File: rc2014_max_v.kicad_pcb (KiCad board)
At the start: 4 copper layers, 101.6 x 50.8 mm, 128 parts, among them J1 M3 Mounting Hole, J2 Conn_01x40, J3 Conn_01x24, J4 USB_B_Micro, J5 AVR-JTAG-10, J6 Pro Bus, J7 PMOD1, J8 PMOD2, J9 UPDI TTL, SW1 SW_Push, SW2 SW_Push, U1 TXB0108PWR, U10 ATtiny1614-SS, U11 5M1270ZT144C5N, U12 93LC46BT-I/OT, U13 IS61LV5128AL-10TLI, U14 Si5351A-B-GT, U15 TXB0108PWR, U16 TXB0108PWR, U18 MIC5356-SGYMME, U2 TXB0108PWR, U3 TXB0108PWR, U4 TXB0108PWR, U5 TXB0108PWR, U6 TXB0108PWR, U7 TXB0108PWR, U8 FT2232H, U9 TPD2EUSB30, X1 KC5032K12.0000C10E00, Y1 25MHZ 8PF

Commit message: formatting and layer stitching
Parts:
- moved U6 0.89 mm to (145.3, 117.3)
- moved U4 0.64 mm to (136.3, 117.3)
- moved R4 0.63 mm to (141.0, 115.1)
- moved C33 0.51 mm to (131.8, 117.3)
- moved U5 0.51 mm to (163.3, 117.3)
- moved U2 0.51 mm to (127.3, 117.3)
- moved J7 0.38 mm to (173.0, 102.9)
- moved R3 0.25 mm to (159.0, 115.1)
- moved J8 0.25 mm to (173.0, 86.1)
- moved R2 0.25 mm to (122.9, 115.1)
- moved RN1 0.25 mm to (122.2, 119.4)
- moved U7 0.13 mm to (154.3, 117.3)
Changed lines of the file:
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@@
   (page A4)
   (layers
-    (0 F.Cu signal)
-    (1 In1.Cu power hide)
+    (0 F.Cu signal hide)
+    (1 In1.Cu power)
     (2 In2.Cu power hide)
     (31 B.Cu signal)
@@
     (aux_axis_origin 0 0)
     (grid_origin 75.438 127.508)
-    (visible_elements FFFFFF7F)
+    (visible_elements FFFFF77F)
     (pcbplotparams
       (layerselection 0x010f0_ffffffff)
@@
     (add_net CLK)
     (add_net CLK2)
-    (add_net CLK2_F)
     (add_net CLK_100Mhz)
     (add_net CLK_1Mhz)
@@
     (add_net "Net-(D13-Pad4)")
     (add_net "Net-(D13-Pad5)")
-    (add_net "Net-(J2-Pad37)")
-    (add_net "Net-(J2-Pad38)")
-    (add_net "Net-(J2-Pad39)")
-    (add_net "Net-(J2-Pad40)")
-    (add_net "Net-(J3-Pad21)")
-    (add_net "Net-(J3-Pad22)")
-    (add_net "Net-(J3-Pad23)")
-    (add_net "Net-(J3-Pad24)")
     (add_net "Net-(J4-Pad2)")
     (add_net "Net-(J4-Pad3)")
-    (add_net "Net-(J5-Pad7)")
-    (add_net "Net-(J5-Pad8)")
     (add_net "Net-(LED1-Pad2)")
     (add_net "Net-(LED2-Pad2)")
@@
     (add_net "Net-(RN2-Pad3)")
     (add_net "Net-(RN2-Pad4)")
-    (add_net "Net-(RN3-Pad4)")
-    (add_net "Net-(RN3-Pad5)")
     (add_net "Net-(RN4-Pad1)")
     (add_net "Net-(RN4-Pad2)")
-    (add_net "Net-(RN4-Pad4)")
-    (add_net "Net-(RN5-Pad4)")
-    (add_net "Net-(U10-Pad11)")
-    (add_net "Net-(U10-Pad12)")
-    (add_net "Net-(U10-Pad13)")
-    (add_net "Net-(U10-Pad2)")
-    (add_net "Net-(U10-Pad3)")
-    (add_net "Net-(U10-Pad4)")
-    (add_net "Net-(U10-Pad5)")
-    (add_net "Net-(U10-Pad6)")
-    (add_net "Net-(U10-Pad7)")
-    (add_net "Net-(U11-Pad106)")
-    (add_net "Net-(U11-Pad119)")
-    (add_net "Net-(U11-Pad120)")
-    (add_net "Net-(U11-Pad121)")
-    (add_net "Net-(U11-Pad122)")
-    (add_net "Net-(U11-Pad129)")
-    (add_net "Net-(U11-Pad130)")
-    (add_net "Net-(U11-Pad131)")
-    (add_net "Net-(U11-Pad132)")
-    (add_net "Net-(U11-Pad133)")
-    (add_net "Net-(U11-Pad32)")
-    (add_net "Net-(U11-Pad72)")
-    (add_net "Net-(U13-Pad1)")
-    (add_net "Net-(U13-Pad2)")
-    (add_net "Net-(U13-Pad21)")
-    (add_net "Net-(U13-Pad22)")
-    (add_net "Net-(U13-Pad23)")
-    (add_net "Net-(U13-Pad24)")
-    (add_net "Net-(U13-Pad25)")
-    (add_net "Net-(U13-Pad39)")
-    (add_net "Net-(U13-Pad40)")
-    (add_net "Net-(U13-Pad41)")
-    (add_net "Net-(U13-Pad42)")
-    (add_net "Net-(U13-Pad43)")
-    (add_net "Net-(U13-Pad44)")
     (add_net "Net-(U14-Pad2)")
     (add_net "Net-(U14-Pad3)")
-    (add_net "Net-(U18-Pad3)")
-    (add_net "Net-(U18-Pad6)")
     (add_net "Net-(U8-Pad2)")
-    (add_net "Net-(U8-Pad21)")
-    (add_net "Net-(U8-Pad22)")
-    (add_net "Net-(U8-Pad23)")
-    (add_net "Net-(U8-Pad24)")
-    (add_net "Net-(U8-Pad26)")
-    (add_net "Net-(U8-Pad27)")
-    (add_net "Net-(U8-Pad28)")
-    (add_net "Net-(U8-Pad29)")
-    (add_net "Net-(U8-Pad3)")
-    (add_net "Net-(U8-Pad30)")
-    (add_net "Net-(U8-Pad32)")
-    (add_net "Net-(U8-Pad33)")
-    (add_net "Net-(U8-Pad34)")
-    (add_net "Net-(U8-Pad36)")
-    (add_net "Net-(U8-Pad38)")
-    (add_net "Net-(U8-Pad39)")
-    (add_net "Net-(U8-Pad40)")
-    (add_net "Net-(U8-Pad41)")
-    (add_net "Net-(U8-Pad43)")
-    (add_net "Net-(U8-Pad44)")
-    (add_net "Net-(U8-Pad45)")
-    (add_net "Net-(U8-Pad46)")
-    (add_net "Net-(U8-Pad48)")
-    (add_net "Net-(U8-Pad49)")
-    (add_net "Net-(U8-Pad50)")
-    (add_net "Net-(U8-Pad52)")
-    (add_net "Net-(U8-Pad53)")
-    (add_net "Net-(U8-Pad54)")
-    (add_net "Net-(U8-Pad55)")
-    (add_net "Net-(U8-Pad57)")
-    (add_net "Net-(U8-Pad58)")
-    (add_net "Net-(U8-Pad59)")
     (add_net OE_A)
     (add_net OE_C)
@@
   )
   (module Capacitor_SMD:C_0805_2012Metric_Pad1.15x1.40mm_HandSolder (layer F.Cu)
-    (at 132.334 117.348 270)
+    (at 131.826 117.348 270)
     (descr "Capacitor SMD 0805 (2012 Metric), square (rectangular) end terminal, IPC_7351 nominal with elongated pad for handsoldering. (Body size source: https://docs.google.com/spreadsheets/d/1BsfQQcO9C6DZCsRaXUlFlo91Tg2WpOkGARC1WS5S8t0/edit?usp=sharing), generated with kicad-footprint-generator")
     (tags "capacitor handsolder")
@@
   )
   (module Resistor_SMD:R_0603_1608Metric_Pad1.05x0.95mm_HandSolder (layer F.Cu)
-    (at 159.258 115.062 90)
+    (at 159.004 115.062 90)
     (descr "Resistor SMD 0603 (1608 Metric), square (rectangular) end terminal, IPC_7351 nominal with elongated pad for handsoldering. (Body size source: http://www.tortai-tech.com/upload/download/2011102023233369053.pdf), generated with kicad-footprint-generator")
     (tags "resistor handsolder")
@@
   )
   (module Resistor_SMD:R_0603_1608Metric_Pad1.05x0.95mm_HandSolder (layer F.Cu)
-    (at 141.605 115.062 90)
+    (at 140.97 115.062 90)
     (descr "Resistor SMD 0603 (1608 Metric), square (rectangular) end terminal, IPC_7351 nominal with elongated pad for handsoldering. (Body size source: http://www.tortai-tech.com/upload/download/2011102023233369053.pdf), generated with kicad-footprint-generator")
     (tags "resistor handsolder")
@@
   )
   (module Resistor_SMD:R_0603_1608Metric_Pad1.05x0.95mm_HandSolder (layer F.Cu)
-    (at 123.19 115.062 90)
+    (at 122.936 115.062 90)
     (descr "Resistor SMD 0603 (1608 Metric), square (rectangular) end terminal, IPC_7351 nominal with elongated pad for handsoldering. (Body size source: http://www.tortai-tech.com/upload/download/2011102023233369053.pdf), generated with kicad-footprint-generator")
     (tags "resistor handsolder")
@@
   )
   (module Resistor_SMD:R_Array_Concave_4x0603 (layer F.Cu)
-    (at 122.428 119.38)
+    (at 122.174 119.38)
     (descr "Thick Film Chip Resistor Array, Wave soldering, Vishay CRA06P (see cra06p.pdf)")
     (tags "resistor array")
@@
   )
   (module Package_SO:TSSOP-20_4.4x6.5mm_P0.65mm (layer F.Cu)
-    (at 154.432 117.348 270)
+    (at 154.305 117.348 270)
     (descr "20-Lead Plastic Thin Shrink Small Outline (ST)-4.4 mm Body [TSSOP] (see Microchip Packaging Specification 00000049BS.pdf)")
     (tags "SSOP 0.65")
@@
   )
   (module Package_SO:TSSOP-20_4.4x6.5mm_P0.65mm (layer F.Cu)
-    (at 163.83 117.348 270)
+    (at 163.322 117.348 270)
     (descr "20-Lead Plastic Thin Shrink Small Outline (ST)-4.4 mm Body [TSSOP] (see Microchip Packaging Specification 00000049BS.pdf)")
     (tags "SSOP 0.65")
@@
   )
   (module Package_SO:TSSOP-20_4.4x6.5mm_P0.65mm (layer F.Cu)
-    (at 146.177 117.348 270)
+    (at 145.288 117.348 270)
     (descr "20-Lead Plastic Thin Shrink Small Outline (ST)-4.4 mm Body [TSSOP] (see Microchip Packaging Specification 00000049BS.pdf)")
     (tags "SSOP 0.65")
@@
   )
   (module Package_SO:TSSOP-20_4.4x6.5mm_P0.65mm (layer F.Cu)
-    (at 136.906 117.348 270)
+    (at 136.271 117.348 270)
     (descr "20-Lead Plastic Thin Shrink Small Outline (ST)-4.4 mm Body [TSSOP] (see Microchip Packaging Specification 00000049BS.pdf)")
     (tags "SSOP 0.65")
@@
   )
   (module Package_SO:TSSOP-20_4.4x6.5mm_P0.65mm (layer F.Cu)
-    (at 127.762 117.348 270)
+    (at 127.254 117.348 270)
     (descr "20-Lead Plastic Thin Shrink Small Outline (ST)-4.4 mm Body [TSSOP] (see Microchip Packaging Specification 00000049BS.pdf)")
     (tags "SSOP 0.65")
@@
   )
   (module Connector_PinSocket_2.54mm:PinSocket_2x06_P2.54mm_Horizontal (layer F.Cu)
-    (at 172.974 86.36)
+    (at 172.974 86.106)
     (descr "Through hole angled socket strip, 2x06, 2.54mm pitch, 8.51mm socket length, double cols (from Kicad 4.0.7), script generated")
     (tags "Through hole angled socket strip THT 2x06 2.54mm double row")
@@
   )
   (module Connector_PinSocket_2.54mm:PinSocket_2x06_P2.54mm_Horizontal (layer F.Cu)
-    (at 172.974 103.251)
+    (at 172.974 102.87)
     (descr "Through hole angled socket strip, 2x06, 2.54mm pitch, 8.51mm socket length, double cols (from Kicad 4.0.7), script generated")
     (tags "Through hole angled socket strip THT 2x06 2.54mm double row")
@@
   (gr_line (start 177.038 127.508) (end 75.438 127.508) (layer Edge.Cuts) (width 0.1))
   (gr_line (start 75.438 127.508) (end 75.438 91.948) (layer Edge.Cuts) (width 0.1))
-  (via (at 84.328 116.332) (size 0.6858) (drill 0.3302) (layers F.Cu B.Cu) (net 198))
   (via (at 84.328 118.364) (size 0.6858) (drill 0.3302) (layers F.Cu B.Cu) (net 1))
-  (via (at 115.316 116.332) (size 0.6858) (drill 0.3302) (layers F.Cu B.Cu) (net 198))
   (via (at 115.316 118.364) (size 0.6858) (drill 0.3302) (layers F.Cu B.Cu) (net 1))
-  (via (at 168.148 116.332) (size 0.6858) (drill 0.3302) (layers F.Cu B.Cu) (net 198))
   (via (at 168.148 118.364) (size 0.6858) (drill 0.3302) (layers F.Cu B.Cu) (net 1))
-  (via (at 132.334 116.332) (size 0.6858) (drill 0.3302) (layers F.Cu B.Cu) (net 198))
   (via (at 132.334 118.364) (size 0.6858) (drill 0.3302) (layers F.Cu B.Cu) (net 1))
+  (via (at 84.328 116.332) (size 0.6858) (drill 0.3302) (layers F.Cu B.Cu) (net 198))
+  (via (at 115.316 116.332) (size 0.6858) (drill 0.3302) (layers F.Cu B.Cu) (net 198))
+  (via (at 168.148 116.332) (size 0.6858) (drill 0.3302) (layers F.Cu B.Cu) (net 198))
+  (via (at 132.334 116.332) (size 0.6858) (drill 0.3302) (layers F.Cu B.Cu) (net 198))
   (zone (net 2) (net_name GND) (layer In2.Cu) (hatch edge 0.508)
     (connect_pads (clearance 0.508))

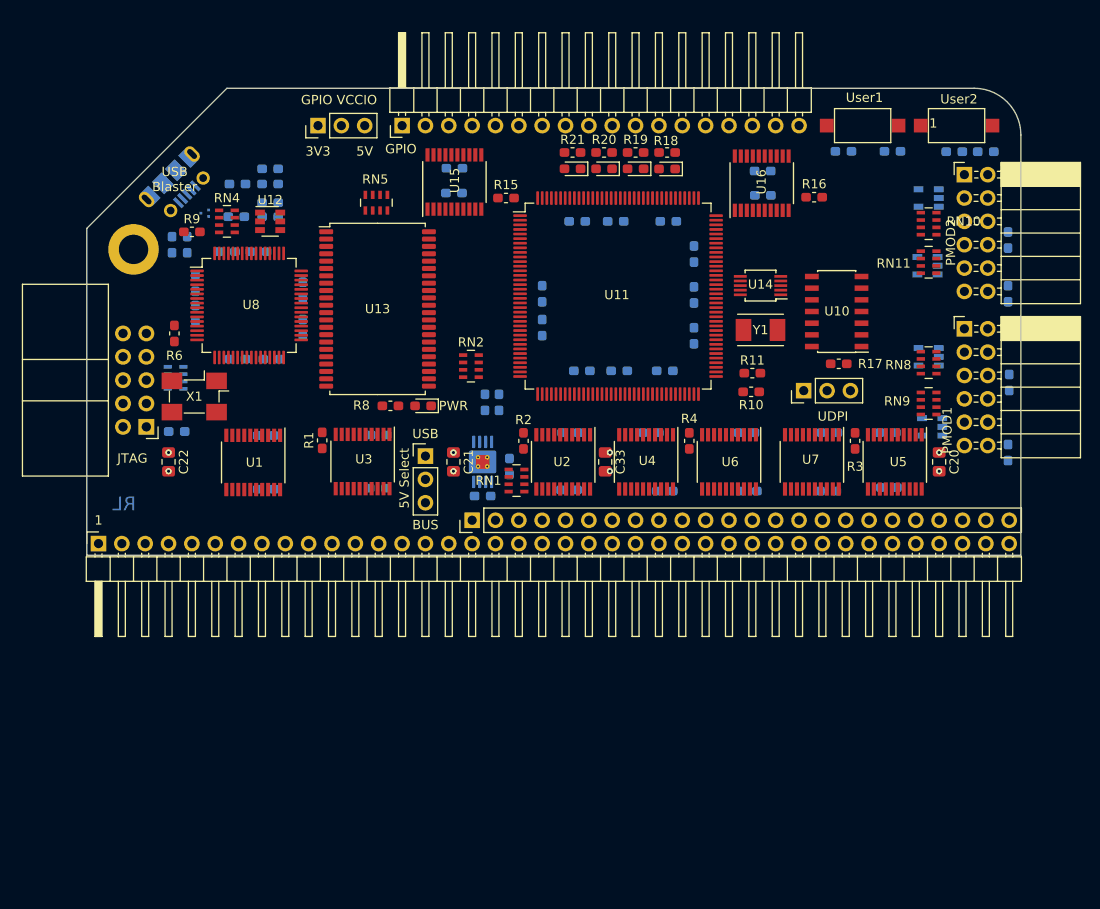
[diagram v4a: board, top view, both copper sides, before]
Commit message: replaced some global pins with hierarchical sheet pins
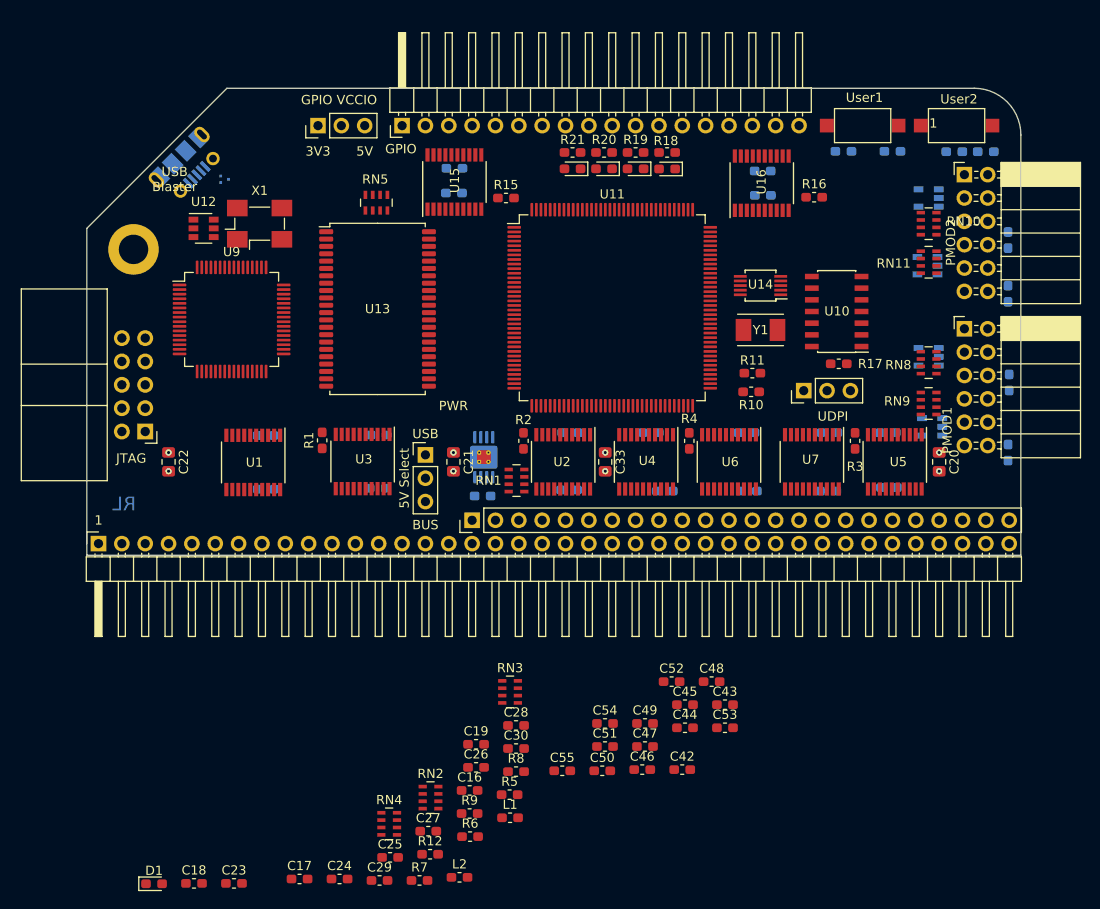
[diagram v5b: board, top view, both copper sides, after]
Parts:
- removed U18: MIC5356-SGYMME, Package_SO:MSOP-8-1EP_3x3mm_P0.65mm_EP2.5x3mm_Mask1.73x2.36mm_ThermalVias
- added U17: MIC5356-SGYMME, Package_SO:MSOP-8-1EP_3x3mm_P0.65mm_EP2.5x3mm_Mask1.73x2.36mm_ThermalVias, B.Cu at (118.6, 116.8)
- C16, C17, C18, C19, C23, C24, C25, C26, C27, C28, C29, C30, C42, C43, C44, C45, C46, C47, C48, C49, C50, C51, C52, C53, C54, C55, L1, L2, RN3: moved to F.Cu
- R12: value 1K -> 2K2; moved to F.Cu
- R5: value 12K -> 1K; moved to F.Cu
- R6: value 1K -> 12K
- R7: value 1M -> 1K; moved to F.Cu
- R8: value 220R -> 1M
- R9: value 2K2 -> 220R
- U8: value FT2232H -> TPD2EUSB30; footprint Package_QFP:TQFP-64_10x10mm_P0.5mm -> Package_TO_SOT_SMD:Texas_DRT-3; moved to B.Cu
- U9: value TPD2EUSB30 -> FT2232H; footprint Package_TO_SOT_SMD:Texas_DRT-3 -> Package_QFP:TQFP-64_10x10mm_P0.5mm; moved to F.Cu
- moved L2 79.2 mm to (116.0, 162.5)
- moved C18 76.5 mm to (87.1, 163.2)
- moved R7 74.2 mm to (111.6, 162.9), turned to 0 degrees
- moved C17 73.6 mm to (98.6, 162.7)
- moved L1 71.8 mm to (121.5, 156.1)
- moved R9 70.1 mm to (117.1, 155.6)
- moved C23 69.7 mm to (91.4, 163.2), turned to 0 degrees
- moved RN4 67.9 mm to (108.3, 156.7), turned to 0 degrees
- moved C19 66.5 mm to (117.8, 148.1)
- moved C16 66.1 mm to (117.1, 153.1)
- moved R5 65.3 mm to (121.4, 153.5), turned to 0 degrees
- moved C29 64.8 mm to (107.3, 162.9), turned to 0 degrees
- moved R6 63.5 mm to (117.1, 158.1), turned to 0 degrees
- moved C30 62.5 mm to (122.1, 148.5)
- moved C26 60.9 mm to (117.8, 150.6)
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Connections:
- net /Max V CPLD and user I/O/Clocks/TX renamed /Max V CPLD/Clocks/TX
- net JTAG_TDI renamed /Max V CPLD/JTAG/TDI
- net JTAG_TDO renamed /Max V CPLD/JTAG/TDO
- net JTAG_TMS renamed /Max V CPLD/JTAG/TMS
- net UPDI renamed /Max V CPLD/Clocks/RX
- J5 pad 1: JTAG_TCK -> /Max V CPLD/JTAG/TCK
- R10 pad 2: SCL -> Net-(R10-Pad2)
- R11 pad 2: SDA -> Net-(R11-Pad2)
- R12 pad 1: GND -> Net-(R12-Pad1)
- R12 pad 2: JTAG_TCK -> Net-(R12-Pad2)
- R5 pad 2: Net-(R5-Pad2) -> /Max V CPLD/JTAG/TCK
- R6 pad 1: 3V3 -> GND
- R7 pad 1: Net-(C23-Pad1) -> 3V3
- R7 pad 2: GND -> Net-(R7-Pad2)
- R8 pad 1: 3V3 -> Net-(C23-Pad1)
- R8 pad 2: Net-(D1-Pad2) -> GND
- R9 pad 1: Net-(R9-Pad1) -> 3V3
- R9 pad 2: Net-(R9-Pad2) -> Net-(D1-Pad2)
- RN2 pad 8: JTAG_TCK -> /Max V CPLD/JTAG/TCK
- RN4 pad 3: Net-(R9-Pad1) -> Net-(R12-Pad1)
- U10 pad 8: SDA -> Net-(R11-Pad2)
- U10 pad 9: SCL -> Net-(R10-Pad2)
- U11 pad 1: SCL -> (no net)
- U11 pad 18: CLK_1Mhz -> /Max V CPLD/Clocks/CLK_100Mhz
- U11 pad 2: SDA -> (no net)
- U11 pad 20: CLK_F -> /Max V CPLD/Clocks/CLK_7_3728_Mhz
- U11 pad 35: JTAG_TCK -> /Max V CPLD/JTAG/TCK
- U11 pad 89: CLK_100Mhz -> /Max V CPLD/Clocks/CLK_1Mhz
- U11 pad 91: CLK_7_3728_Mhz -> CLK_F
- U12 pad 1: Net-(R9-Pad1) -> Net-(R12-Pad1)
- U12 pad 3: Net-(R9-Pad2) -> Net-(R12-Pad2)
- U14 pad 10: CLK_100Mhz -> /Max V CPLD/Clocks/CLK_100Mhz
- U14 pad 4: SCL -> Net-(R10-Pad2)
- U14 pad 5: SDA -> Net-(R11-Pad2)
- U14 pad 6: CLK_1Mhz -> /Max V CPLD/Clocks/CLK_1Mhz
- U14 pad 9: CLK_7_3728_Mhz -> /Max V CPLD/Clocks/CLK_7_3728_Mhz
- U8 pad 1: GND -> Net-(J4-Pad3)
- U8 pad 2: Net-(U8-Pad2) -> Net-(J4-Pad2)
- U8 pad 3: (no net) -> GND
- U9 pad 1: Net-(J4-Pad3) -> GND
- U9 pad 2: Net-(J4-Pad2) -> Net-(U9-Pad2)
- U9 pad 3: GND -> (no net)
- X1 pad 3: Net-(U8-Pad2) -> Net-(U9-Pad2)

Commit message: recovered layout
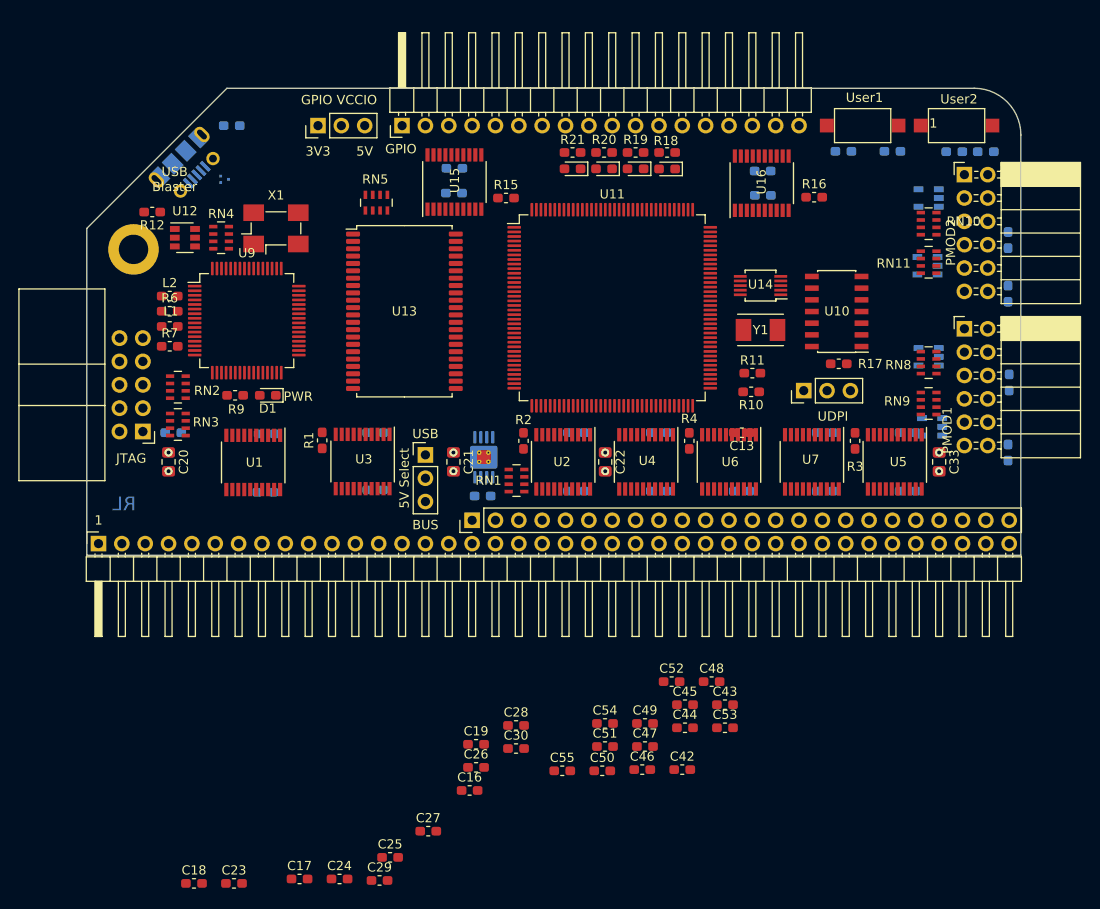
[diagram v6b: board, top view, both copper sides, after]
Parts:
- C13: moved to F.Cu
- R5, R8: moved to B.Cu
- moved C20 83.8 mm to (84.3, 117.3)
- moved R8 76.8 mm to (91.2, 80.8)
- moved R12 76.1 mm to (82.5, 90.2), turned to 180 degrees
- moved L2 70.6 mm to (84.5, 99.3)
- moved RN4 66.3 mm to (90.0, 93.0)
- moved R6 65.8 mm to (84.5, 101.0)
- moved L1 65.0 mm to (84.5, 102.6)
- moved R7 64.1 mm to (84.5, 104.8)
- moved D1 54.5 mm to (95.1, 110.1), turned to 180 degrees
- moved R5 53.8 mm to (84.8, 114.2), turned to 180 degrees
- moved RN2 52.4 mm to (85.3, 109.2), turned to 180 degrees
- moved R9 52.2 mm to (91.6, 110.1)
- moved C22 47.5 mm to (131.8, 117.3)
- moved RN3 46.4 mm to (85.3, 113.3)
- moved C33 36.3 mm to (168.1, 117.3)
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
